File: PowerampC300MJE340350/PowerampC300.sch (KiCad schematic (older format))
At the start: 109 parts, among them J1 Conn_01x02, J2 Conn_01x02, J3 Conn_01x02, J4 Conn_01x01, J5 Conn_01x01, J6 Conn_01x01, J7 Conn_01x01, J8 Conn_01x02, J9 Conn_Coaxial, Q1 2N5551, Q10 MJE15033, Q11 MJE15032, Q12 MJE15032, Q13 2N5551, Q14 2N5401, Q15 MJE15032, Q16 MJE15033, Q17 MJL3281A, Q18 MJL1302A, Q19 MJL3281A, Q2 2N5551, Q20 MJL1302A, Q21 MJL3281A, Q22 MJL1302A, Q23 MJL3281A, Q24 MJL1302A, Q3 2N5401, Q4 2N5401, Q5 2N5551, Q6 2N5551, Q7 2N5551, Q8 2N5401, Q9 2N5401

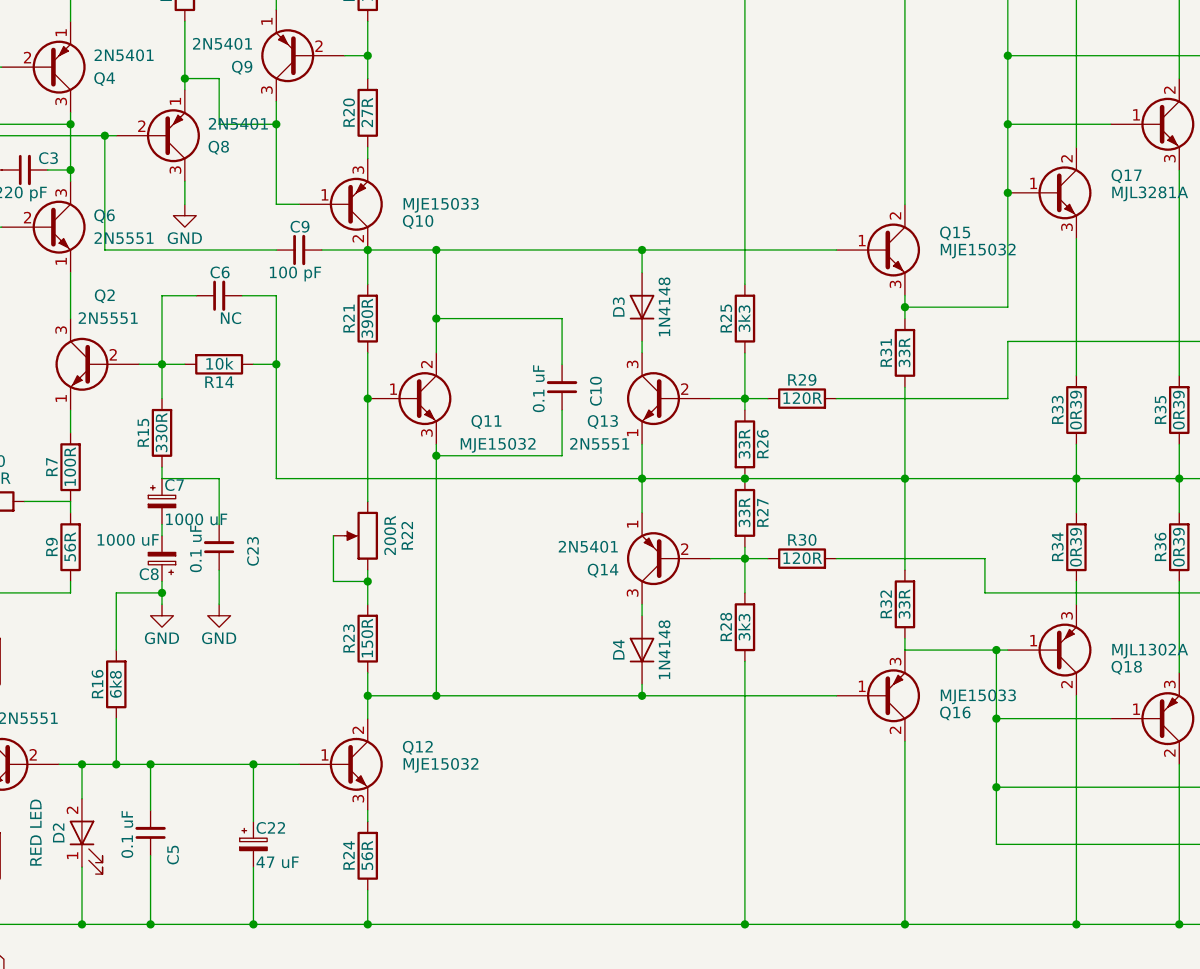
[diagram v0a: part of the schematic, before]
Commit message: Some more layout changed and XlrtoBal fix
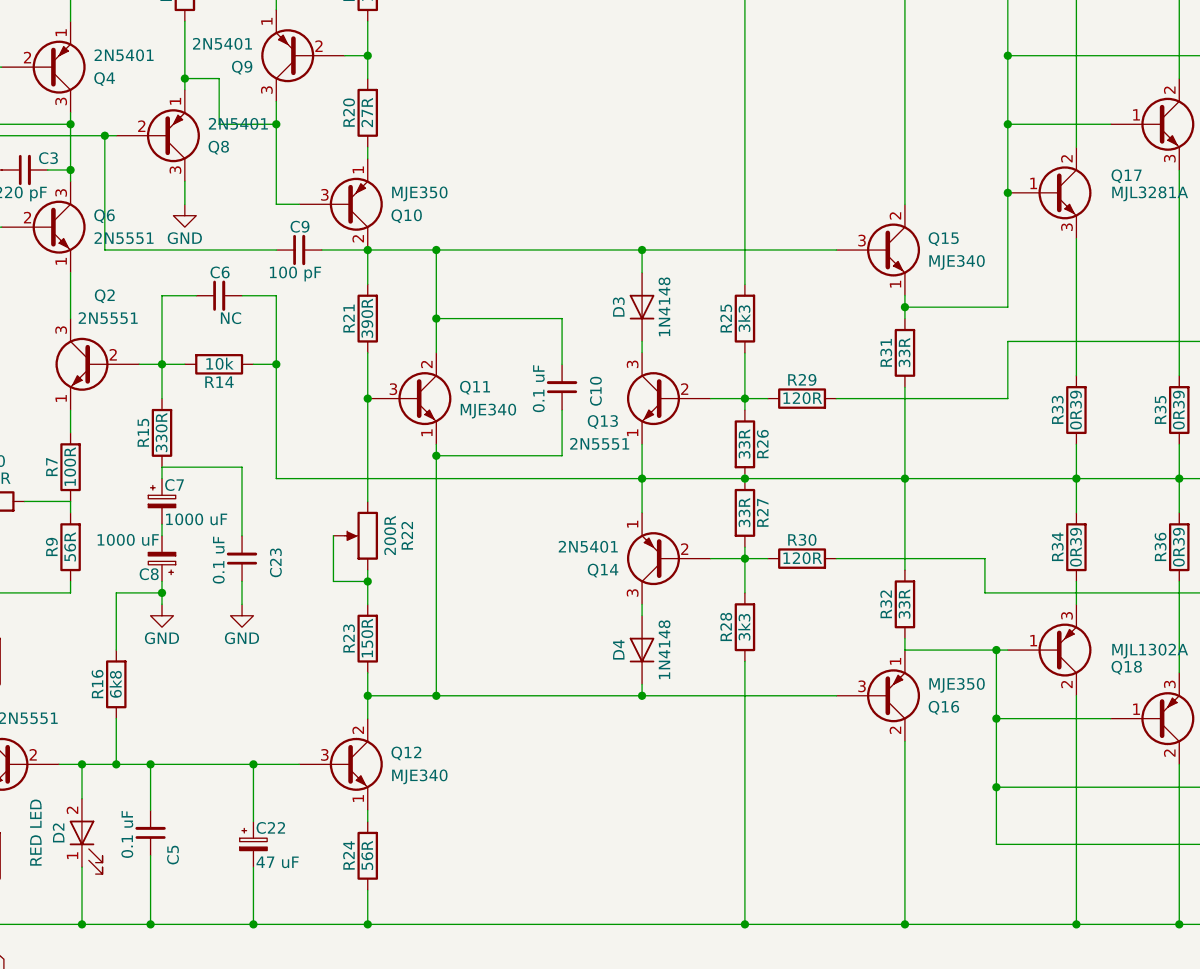
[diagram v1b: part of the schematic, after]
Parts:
- removed Q10, Q16: MJE15033, TO_SOT_Packages_THT:TO-220-3_Vertical, symbol TIP42C
- removed Q11, Q12, Q15: MJE15032, TO_SOT_Packages_THT:TO-220-3_Vertical, symbol TIP41C
- added Q10, Q16: MJE350, TO_SOT_Packages_THT:TO-126_Vertical, symbol Q_PNP_ECB
- added Q11, Q12, Q15: MJE340, TO_SOT_Packages_THT:TO-126_Vertical, symbol Q_NPN_ECB
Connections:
- net +48V: now also Q15.2 (C)
- net -48V: now also Q16.2 (C)
- net at C22.1, C5.2, D2.2 (A)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: now also Q12.3 (B)
- net at R24.2: now also Q12.1 (E)
- net at C10.1, D4.1 (K), R23.1: now also Q11.1 (E), Q12.2 (C), Q16.3 (B)
- net at R21.1, R22.3: now also Q11.3 (B)
- net at Q8.1 (E), Q9.3 (C), R17.1: now also Q10.3 (B)
- net at R20.1: now also Q10.1 (E)
- net at C10.2, C9.2, D3.2 (A)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: now also Q10.2 (C), Q11.2 (C), Q15.3 (B)
- net at Q17.1 (B), Q19.1 (B), Q21.1 (B)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: now also Q15.1 (E)
- net at Q18.1 (B), Q20.1 (B), Q22.1 (B)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: now also Q16.1 (E)
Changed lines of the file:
@@
 	10800 4750 10800 4900
-$Comp
-L TIP41C Q12
-U 1 1 5F4FB282
-P 3800 5450
-F 0 "Q12" H 4050 5525 50  0000 L CNN
-F 1 "MJE15032" H 4050 5450 50  0000 L CNN
-F 2 "TO_SOT_Packages_THT:TO-220-3_Vertical" H 4050 5375 50  0001 L CIN
-F 3 "" H 3800 5450 50  0001 L CNN
-	1    3800 5450
-	1    0    0    -1
-$EndComp
-$Comp
-L TIP42C Q16
-U 1 1 5F4FB50E
-P 6150 5150
-F 0 "Q16" H 6400 5225 50  0000 L CNN
-F 1 "MJE15033" H 6400 5150 50  0000 L CNN
-F 2 "TO_SOT_Packages_THT:TO-220-3_Vertical" H 6400 5075 50  0001 L CIN
-F 3 "" H 6150 5150 50  0001 L CNN
-	1    6150 5150
-	1    0    0    1
-$EndComp
-$Comp
-L TIP41C Q11
-U 1 1 5F4FBF00
-P 4100 3850
-F 0 "Q11" H 4350 3750 50  0000 L CNN
-F 1 "MJE15032" H 4300 3650 50  0000 L CNN
-F 2 "TO_SOT_Packages_THT:TO-220-3_Vertical" H 4350 3775 50  0001 L CIN
-F 3 "" H 4100 3850 50  0001 L CNN
-	1    4100 3850
-	1    0    0    -1
-$EndComp
-$Comp
-L TIP41C Q15
-U 1 1 5F4FC974
-P 6150 3200
-F 0 "Q15" H 6400 3275 50  0000 L CNN
-F 1 "MJE15032" H 6400 3200 50  0000 L CNN
-F 2 "TO_SOT_Packages_THT:TO-220-3_Vertical" H 6400 3125 50  0001 L CIN
-F 3 "" H 6150 3200 50  0001 L CNN
-	1    6150 3200
-	1    0    0    -1
-$EndComp
-$Comp
-L TIP42C Q10
-U 1 1 5F500035
-P 3800 3000
-F 0 "Q10" H 4050 3075 50  0000 L CNN
-F 1 "MJE15033" H 4050 3000 50  0000 L CNN
-F 2 "TO_SOT_Packages_THT:TO-220-3_Vertical" H 4050 2925 50  0001 L CIN
-F 3 "" H 3800 3000 50  0001 L CNN
-	1    3800 3000
-	1    0    0    1
-$EndComp
 $Comp
 L L L1
@@
 Connection ~ 3400 6150
 $Comp
+L Q_PNP_ECB Q10
+U 1 1 5F6462BC
+P 3800 3000
+F 0 "Q10" H 4000 3050 50  0000 L CNN
+F 1 "MJE350" H 4000 2950 50  0000 L CNN
+F 2 "TO_SOT_Packages_THT:TO-126_Vertical" H 4000 3100 50  0001 C CNN
+F 3 "" H 3800 3000 50  0001 C CNN
+	1    3800 3000
+	1    0    0    1
+$EndComp
+$Comp
+L Q_NPN_ECB Q15
+U 1 1 5F646890
+P 6150 3200
+F 0 "Q15" H 6350 3250 50  0000 L CNN
+F 1 "MJE340" H 6350 3150 50  0000 L CNN
+F 2 "TO_SOT_Packages_THT:TO-126_Vertical" H 6350 3300 50  0001 C CNN
+F 3 "" H 6150 3200 50  0001 C CNN
+	1    6150 3200
+	1    0    0    -1
+$EndComp
+$Comp
+L Q_PNP_ECB Q16
+U 1 1 5F647AEA
+P 6150 5150
+F 0 "Q16" H 6350 5200 50  0000 L CNN
+F 1 "MJE350" H 6350 5100 50  0000 L CNN
+F 2 "TO_SOT_Packages_THT:TO-126_Vertical" H 6350 5250 50  0001 C CNN
+F 3 "" H 6150 5150 50  0001 C CNN
+	1    6150 5150
+	1    0    0    1
+$EndComp
+$Comp
+L Q_NPN_ECB Q12
+U 1 1 5F648226
+P 3800 5450
+F 0 "Q12" H 4000 5500 50  0000 L CNN
+F 1 "MJE340" H 4000 5400 50  0000 L CNN
+F 2 "TO_SOT_Packages_THT:TO-126_Vertical" H 4000 5550 50  0001 C CNN
+F 3 "" H 3800 5450 50  0001 C CNN
+	1    3800 5450
+	1    0    0    -1
+$EndComp
+$Comp
+L Q_NPN_ECB Q11
+U 1 1 5F6486B6
+P 4100 3850
+F 0 "Q11" H 4300 3900 50  0000 L CNN
+F 1 "MJE340" H 4300 3800 50  0000 L CNN
+F 2 "TO_SOT_Packages_THT:TO-126_Vertical" H 4300 3950 50  0001 C CNN
+F 3 "" H 4100 3850 50  0001 C CNN
+	1    4100 3850
+	1    0    0    -1
+$EndComp
+$Comp
 L C_Small C23
-U 1 1 5F648182
-P 3250 4500
-F 0 "C23" V 3100 4450 50  0000 L CNN
-F 1 "0.1 uF" V 3350 4400 50  0000 L CNN
-F 2 "Capacitors_THT:C_Axial_L3.8mm_D2.6mm_P10.00mm_Horizontal" H 3250 4500 50  0001 C CNN
-F 3 "" H 3250 4500 50  0001 C CNN
-F 4 "C390130" V 3250 4500 60  0001 C CNN "LCSC"
-	1    3250 4500
+U 1 1 5F646F75
+P 3350 4550
+F 0 "C23" V 3200 4500 50  0000 L CNN
+F 1 "0.1 uF" V 3450 4450 50  0000 L CNN
+F 2 "Capacitors_THT:C_Axial_L3.8mm_D2.6mm_P10.00mm_Horizontal" H 3350 4550 50  0001 C CNN
+F 3 "" H 3350 4550 50  0001 C CNN
+F 4 "C390130" V 3350 4550 60  0001 C CNN "LCSC"
+	1    3350 4550
 	-1   0    0    1
 $EndComp
 $Comp
 L GND #PWR7
-U 1 1 5F648447
-P 3250 4750
-F 0 "#PWR7" H 3250 4500 50  0001 C CNN
-F 1 "GND" H 3250 4600 50  0000 C CNN
-F 2 "" H 3250 4750 50  0001 C CNN
-F 3 "" H 3250 4750 50  0001 C CNN
-	1    3250 4750
-	1    0    0    -1
-$EndComp
-Wire Wire Line
-	3250 4750 3250 4600
-Wire Wire Line
-	3000 4200 3250 4200
-Wire Wire Line
-	3250 4200 3250 4400
+U 1 1 5F64731E
+P 3350 4750
+F 0 "#PWR7" H 3350 4500 50  0001 C CNN
+F 1 "GND" H 3350 4600 50  0000 C CNN
+F 2 "" H 3350 4750 50  0001 C CNN
+F 3 "" H 3350 4750 50  0001 C CNN
+	1    3350 4750
+	1    0    0    -1
+$EndComp
+Wire Wire Line
+	3350 4750 3350 4650
+Wire Wire Line
+	3000 4150 3350 4150
+Wire Wire Line
+	3350 4150 3350 4450
 $EndSCHEMATC

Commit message: JLCPCB order 2020-09-21
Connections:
- net GND: now also C11.1; no longer R41.1
- net at C6.2, D5.2 (A), D6.1 (K)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: now also R41.2; no longer C11.2
- new net: C11.2, R41.1
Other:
- moved on the sheet: C11, R41
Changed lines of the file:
@@
 $EndComp
 $Comp
-L GND #PWR2
+L GND #PWR01
 U 1 1 5F3B0902
 P 1000 4100
-F 0 "#PWR2" H 1000 3850 50  0001 C CNN
+F 0 "#PWR01" H 1000 3850 50  0001 C CNN
 F 1 "GND" H 1000 3950 50  0000 C CNN
 F 2 "" H 1000 4100 50  0001 C CNN
@@
 $EndComp
 $Comp
-L GND #PWR4
+L GND #PWR02
 U 1 1 5F3B09D1
 P 1500 4100
-F 0 "#PWR4" H 1500 3850 50  0001 C CNN
+F 0 "#PWR02" H 1500 3850 50  0001 C CNN
 F 1 "GND" H 1500 3950 50  0000 C CNN
 F 2 "" H 1500 4100 50  0001 C CNN
@@
 $EndComp
 $Comp
-L GND #PWR1
+L GND #PWR03
 U 1 1 5F3B1EB5
 P 950 3400
-F 0 "#PWR1" H 950 3150 50  0001 C CNN
+F 0 "#PWR03" H 950 3150 50  0001 C CNN
 F 1 "GND" H 950 3250 50  0000 C CNN
 F 2 "" H 950 3400 50  0001 C CNN
@@
 $EndComp
 $Comp
-L GND #PWR3
+L GND #PWR04
 U 1 1 5F3B1F70
 P 1300 3400
-F 0 "#PWR3" H 1300 3150 50  0001 C CNN
+F 0 "#PWR04" H 1300 3150 50  0001 C CNN
 F 1 "GND" H 1300 3250 50  0000 C CNN
 F 2 "" H 1300 3400 50  0001 C CNN
@@
 $EndComp
 $Comp
-L GND #PWR5
+L GND #PWR05
 U 1 1 5F3B40A9
 P 3000 4750
-F 0 "#PWR5" H 3000 4500 50  0001 C CNN
+F 0 "#PWR05" H 3000 4500 50  0001 C CNN
 F 1 "GND" H 3000 4600 50  0000 C CNN
 F 2 "" H 3000 4750 50  0001 C CNN
@@
 $EndComp
 $Comp
-L GND #PWR6
+L GND #PWR06
 U 1 1 5F3B638D
 P 3100 3000
-F 0 "#PWR6" H 3100 2750 50  0001 C CNN
+F 0 "#PWR06" H 3100 2750 50  0001 C CNN
 F 1 "GND" H 3100 2850 50  0000 C CNN
 F 2 "" H 3100 3000 50  0001 C CNN
@@
 L C_Small C11
 U 1 1 5F3C6684
-P 9450 4400
-F 0 "C11" V 9300 4350 50  0000 L CNN
-F 1 "0.1 uF" V 9550 4300 50  0000 L CNN
-F 2 "Capacitors_THT:C_Axial_L3.8mm_D2.6mm_P10.00mm_Horizontal" H 9450 4400 50  0001 C CNN
-F 3 "" H 9450 4400 50  0001 C CNN
-F 4 "C390130" V 9450 4400 60  0001 C CNN "LCSC"
-	1    9450 4400
+P 9450 4700
+F 0 "C11" V 9300 4650 50  0000 L CNN
+F 1 "0.1 uF" V 9550 4600 50  0000 L CNN
+F 2 "Capacitors_THT:C_Axial_L3.8mm_D2.6mm_P10.00mm_Horizontal" H 9450 4700 50  0001 C CNN
+F 3 "" H 9450 4700 50  0001 C CNN
+F 4 "C390130" V 9450 4700 60  0001 C CNN "LCSC"
+	1    9450 4700
 	-1   0    0    1
 $EndComp
@@
 L R R41
 U 1 1 5F3C6B8C
-P 9450 4700
-F 0 "R41" V 9530 4700 50  0000 C CNN
-F 1 "4R7" V 9450 4700 50  0000 C CNN
-F 2 "Resistors_THT:R_Axial_DIN0309_L9.0mm_D3.2mm_P12.70mm_Horizontal" V 9380 4700 50  0001 C CNN
-F 3 "" H 9450 4700 50  0001 C CNN
-F 4 "C57725" V 9450 4700 60  0001 C CNN "LCSC"
-	1    9450 4700
-	-1   0    0    1
-$EndComp
-$Comp
-L GND #PWR11
+P 9450 4400
+F 0 "R41" V 9530 4400 50  0000 C CNN
+F 1 "4R7" V 9450 4400 50  0000 C CNN
+F 2 "Resistors_THT:R_Axial_DIN0309_L9.0mm_D3.2mm_P12.70mm_Horizontal" V 9380 4400 50  0001 C CNN
+F 3 "" H 9450 4400 50  0001 C CNN
+F 4 "C57725" V 9450 4400 60  0001 C CNN "LCSC"
+	1    9450 4400
+	-1   0    0    1
+$EndComp
+$Comp
+L GND #PWR07
 U 1 1 5F3C725A
 P 9450 4900
-F 0 "#PWR11" H 9450 4650 50  0001 C CNN
+F 0 "#PWR07" H 9450 4650 50  0001 C CNN
 F 1 "GND" H 9450 4750 50  0000 C CNN
 F 2 "" H 9450 4900 50  0001 C CNN
@@
 $EndComp
 $Comp
-L GND #PWR10
+L GND #PWR08
 U 1 1 5F3C82FF
 P 9150 6100
-F 0 "#PWR10" H 9150 5850 50  0001 C CNN
+F 0 "#PWR08" H 9150 5850 50  0001 C CNN
 F 1 "GND" H 9150 5950 50  0000 C CNN
 F 2 "" H 9150 6100 50  0001 C CNN
@@
 $EndComp
 $Comp
-L GND #PWR9
+L GND #PWR09
 U 1 1 5F3C9FC4
 P 9100 2800
-F 0 "#PWR9" H 9100 2550 50  0001 C CNN
+F 0 "#PWR09" H 9100 2550 50  0001 C CNN
 F 1 "GND" H 9100 2650 50  0000 C CNN
 F 2 "" H 9100 2800 50  0001 C CNN
@@
 OUTPUT
 $Comp
-L GND #PWR15
+L GND #PWR010
 U 1 1 5F3D5C64
 P 10700 3450
-F 0 "#PWR15" H 10700 3200 50  0001 C CNN
+F 0 "#PWR010" H 10700 3200 50  0001 C CNN
 F 1 "GND" H 10700 3300 50  0000 C CNN
 F 2 "" H 10700 3450 50  0001 C CNN
@@
 $EndComp
 $Comp
-L GND #PWR14
+L GND #PWR011
 U 1 1 5F3D7497
 P 10650 5700
-F 0 "#PWR14" H 10650 5450 50  0001 C CNN
+F 0 "#PWR011" H 10650 5450 50  0001 C CNN
 F 1 "GND" H 10650 5550 50  0000 C CNN
 F 2 "" H 10650 5700 50  0001 C CNN
@@
 $EndComp
 $Comp
-L GND #PWR16
+L GND #PWR012
 U 1 1 5F3D76F6
 P 10800 4900
-F 0 "#PWR16" H 10800 4650 50  0001 C CNN
+F 0 "#PWR012" H 10800 4650 50  0001 C CNN
 F 1 "GND" H 10800 4750 50  0000 C CNN
 F 2 "" H 10800 4900 50  0001 C CNN
@@
 $EndComp
 $Comp
-L GND #PWR13
+L GND #PWR013
 U 1 1 5F3DED23
 P 10500 2350
-F 0 "#PWR13" H 10500 2100 50  0001 C CNN
+F 0 "#PWR013" H 10500 2100 50  0001 C CNN
 F 1 "GND" H 10500 2200 50  0000 C CNN
 F 2 "" H 10500 2350 50  0001 C CNN
@@
 INPUT
 $Comp
-L GND #PWR12
+L GND #PWR014
 U 1 1 5F3DF546
 P 10100 1800
-F 0 "#PWR12" H 10100 1550 50  0001 C CNN
+F 0 "#PWR014" H 10100 1550 50  0001 C CNN
 F 1 "GND" H 10100 1650 50  0000 C CNN
 F 2 "" H 10100 1800 50  0001 C CNN
@@
 Connection ~ 8250 6150
 Wire Wire Line
-	9450 4900 9450 4850
-Wire Wire Line
-	9450 4550 9450 4500
+	9450 4900 9450 4800
 Wire Wire Line
 	8950 5000 8950 6150
@@
 Connection ~ 8900 2350
 Wire Wire Line
-	9450 3950 9450 4300
+	9450 3950 9450 4250
 Connection ~ 9450 4200
 Connection ~ 9150 5600
@@
 	9350 1100 9100 1100
 $Comp
-L GND #PWR8
+L GND #PWR015
 U 1 1 5F401BCA
 P 8750 1200
-F 0 "#PWR8" H 8750 950 50  0001 C CNN
+F 0 "#PWR015" H 8750 950 50  0001 C CNN
 F 1 "GND" H 8750 1050 50  0000 C CNN
 F 2 "" H 8750 1200 50  0001 C CNN
@@
 Connection ~ 3400 6150
 $Comp
+L C_Small C23
+U 1 1 5F648182
+P 3250 4500
+F 0 "C23" V 3100 4450 50  0000 L CNN
+F 1 "0.1 uF" V 3350 4400 50  0000 L CNN
+F 2 "Capacitors_THT:C_Axial_L3.8mm_D2.6mm_P10.00mm_Horizontal" H 3250 4500 50  0001 C CNN
+F 3 "" H 3250 4500 50  0001 C CNN
+F 4 "C390130" V 3250 4500 60  0001 C CNN "LCSC"
+	1    3250 4500
+	-1   0    0    1
+$EndComp
+$Comp
+L GND #PWR016
+U 1 1 5F648447
+P 3250 4750
+F 0 "#PWR016" H 3250 4500 50  0001 C CNN
+F 1 "GND" H 3250 4600 50  0000 C CNN
+F 2 "" H 3250 4750 50  0001 C CNN
+F 3 "" H 3250 4750 50  0001 C CNN
+	1    3250 4750
+	1    0    0    -1
+$EndComp
+Wire Wire Line
+	3250 4750 3250 4600
+Wire Wire Line
+	3000 4200 3250 4200
+Wire Wire Line
+	3250 4200 3250 4400
+Wire Wire Line
+	9450 4550 9450 4600
+$Comp
+L Q_NPN_ECB Q12
+U 1 1 5F6862D9
+P 3800 5450
+F 0 "Q12" H 4000 5500 50  0000 L CNN
+F 1 "MJE340" H 4000 5400 50  0000 L CNN
+F 2 "TO_SOT_Packages_THT:TO-126_Vertical" H 4000 5550 50  0001 C CNN
+F 3 "" H 3800 5450 50  0001 C CNN
+	1    3800 5450
+	1    0    0    -1
+$EndComp
+$Comp
+L Q_NPN_ECB Q11
+U 1 1 5F6865B0
+P 4100 3850
+F 0 "Q11" H 4300 3900 50  0000 L CNN
+F 1 "MJE340" H 4300 3800 50  0000 L CNN
+F 2 "TO_SOT_Packages_THT:TO-126_Vertical" H 4300 3950 50  0001 C CNN
+F 3 "" H 4100 3850 50  0001 C CNN
+	1    4100 3850
+	1    0    0    -1
+$EndComp
+$Comp
+L Q_NPN_ECB Q15
+U 1 1 5F686879
+P 6150 3200
+F 0 "Q15" H 6350 3250 50  0000 L CNN
+F 1 "MJE340" H 6350 3150 50  0000 L CNN
+F 2 "TO_SOT_Packages_THT:TO-126_Vertical" H 6350 3300 50  0001 C CNN
+F 3 "" H 6150 3200 50  0001 C CNN
+	1    6150 3200
+	1    0    0    -1
+$EndComp
+$Comp
 L Q_PNP_ECB Q10
-U 1 1 5F6462BC
+U 1 1 5F686C2D
 P 3800 3000
 F 0 "Q10" H 4000 3050 50  0000 L CNN
@@
 $EndComp
 $Comp
-L Q_NPN_ECB Q15
-U 1 1 5F646890
-P 6150 3200
-F 0 "Q15" H 6350 3250 50  0000 L CNN
-F 1 "MJE340" H 6350 3150 50  0000 L CNN
-F 2 "TO_SOT_Packages_THT:TO-126_Vertical" H 6350 3300 50  0001 C CNN
-F 3 "" H 6150 3200 50  0001 C CNN
-	1    6150 3200
-	1    0    0    -1
-$EndComp
-$Comp
 L Q_PNP_ECB Q16
-U 1 1 5F647AEA
+U 1 1 5F686F0E
 P 6150 5150
 F 0 "Q16" H 6350 5200 50  0000 L CNN
@@
 	1    0    0    1
 $EndComp
-$Comp
-L Q_NPN_ECB Q12
-U 1 1 5F648226
-P 3800 5450
-F 0 "Q12" H 4000 5500 50  0000 L CNN
-F 1 "MJE340" H 4000 5400 50  0000 L CNN
-F 2 "TO_SOT_Packages_THT:TO-126_Vertical" H 4000 5550 50  0001 C CNN
-F 3 "" H 3800 5450 50  0001 C CNN
-	1    3800 5450
-	1    0    0    -1
-$EndComp
-$Comp
-L Q_NPN_ECB Q11
-U 1 1 5F6486B6
-P 4100 3850
-F 0 "Q11" H 4300 3900 50  0000 L CNN
-F 1 "MJE340" H 4300 3800 50  0000 L CNN
-F 2 "TO_SOT_Packages_THT:TO-126_Vertical" H 4300 3950 50  0001 C CNN
-F 3 "" H 4100 3850 50  0001 C CNN
-	1    4100 3850
-	1    0    0    -1
-$EndComp
-$Comp
-L C_Small C23
-U 1 1 5F646F75
-P 3350 4550
-F 0 "C23" V 3200 4500 50  0000 L CNN
-F 1 "0.1 uF" V 3450 4450 50  0000 L CNN
-F 2 "Capacitors_THT:C_Axial_L3.8mm_D2.6mm_P10.00mm_Horizontal" H 3350 4550 50  0001 C CNN
-F 3 "" H 3350 4550 50  0001 C CNN
-F 4 "C390130" V 3350 4550 60  0001 C CNN "LCSC"
-	1    3350 4550
-	-1   0    0    1
-$EndComp
-$Comp
-L GND #PWR7
-U 1 1 5F64731E
-P 3350 4750
-F 0 "#PWR7" H 3350 4500 50  0001 C CNN
-F 1 "GND" H 3350 4600 50  0000 C CNN
-F 2 "" H 3350 4750 50  0001 C CNN
-F 3 "" H 3350 4750 50  0001 C CNN
-	1    3350 4750
-	1    0    0    -1
-$EndComp
-Wire Wire Line
-	3350 4750 3350 4650
-Wire Wire Line
-	3000 4150 3350 4150
-Wire Wire Line
-	3350 4150 3350 4450
 $EndSCHEMATC
